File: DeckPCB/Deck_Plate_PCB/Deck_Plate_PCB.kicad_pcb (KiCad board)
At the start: 2 copper layers, 101.6 x 53.3 mm, 18 parts, among them J1 DB37_Female_MountingHoles, J2 DB15_Female_MountingHoles, P1 Digital, P10 CONN_01X01, P11 CONN_01X01, P12 CONN_01X01, P13 CONN_01X01, P2 Power, P3 Analog, P4 Analog, P5 PWM, P6 PWM, P7 Communication, P8 CONN_01X01, P9 CONN_01X01, U1 Adafruit_INA219_Breakout, U2 LM2576T-5, U3 D24V25F9

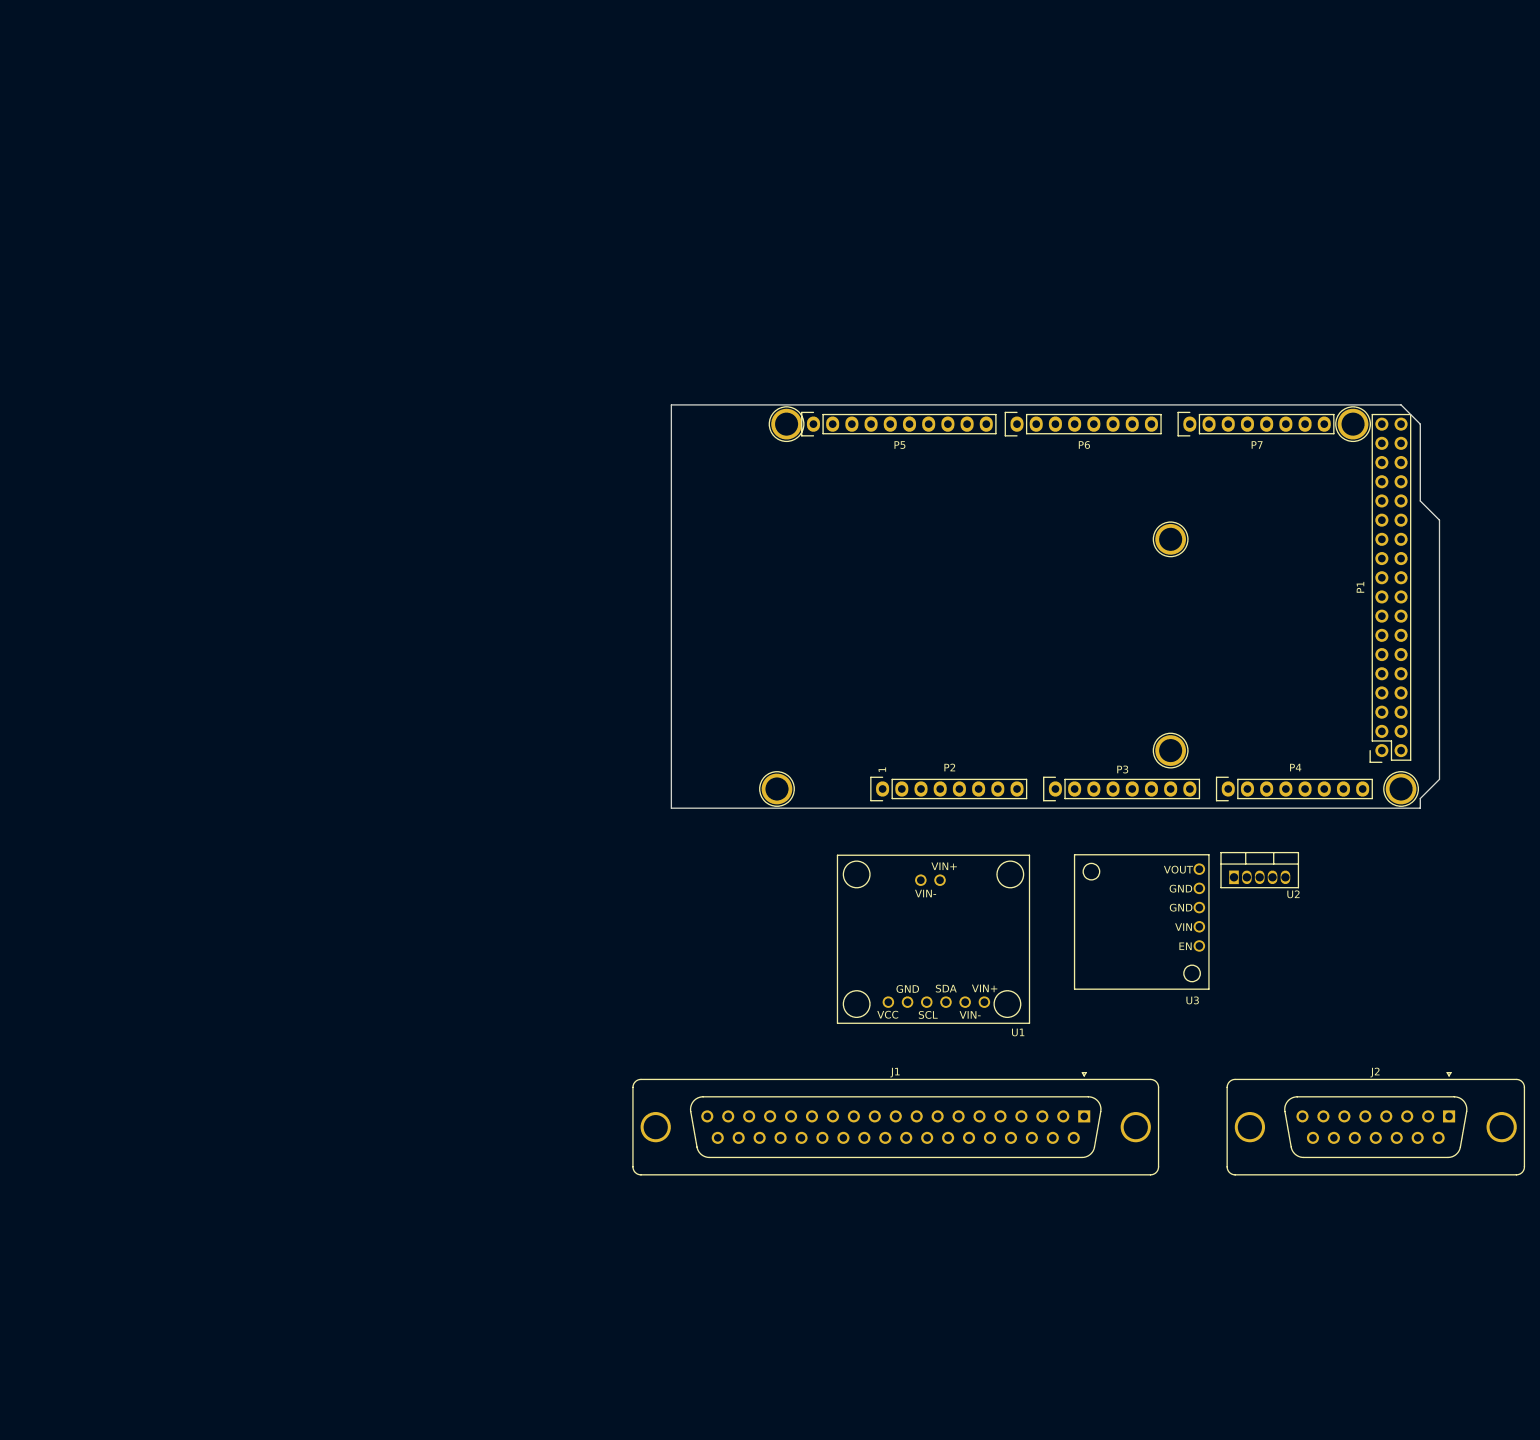
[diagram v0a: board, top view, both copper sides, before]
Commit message: Deleted OnBoardPCB folder, replaced with Deck_Plate_PCB. This should be treated as the MASTER PCB reference from here on out. Added all sensor footprints and symbols as custom parts which are part of a custom DECK_PLATE_PCB library.
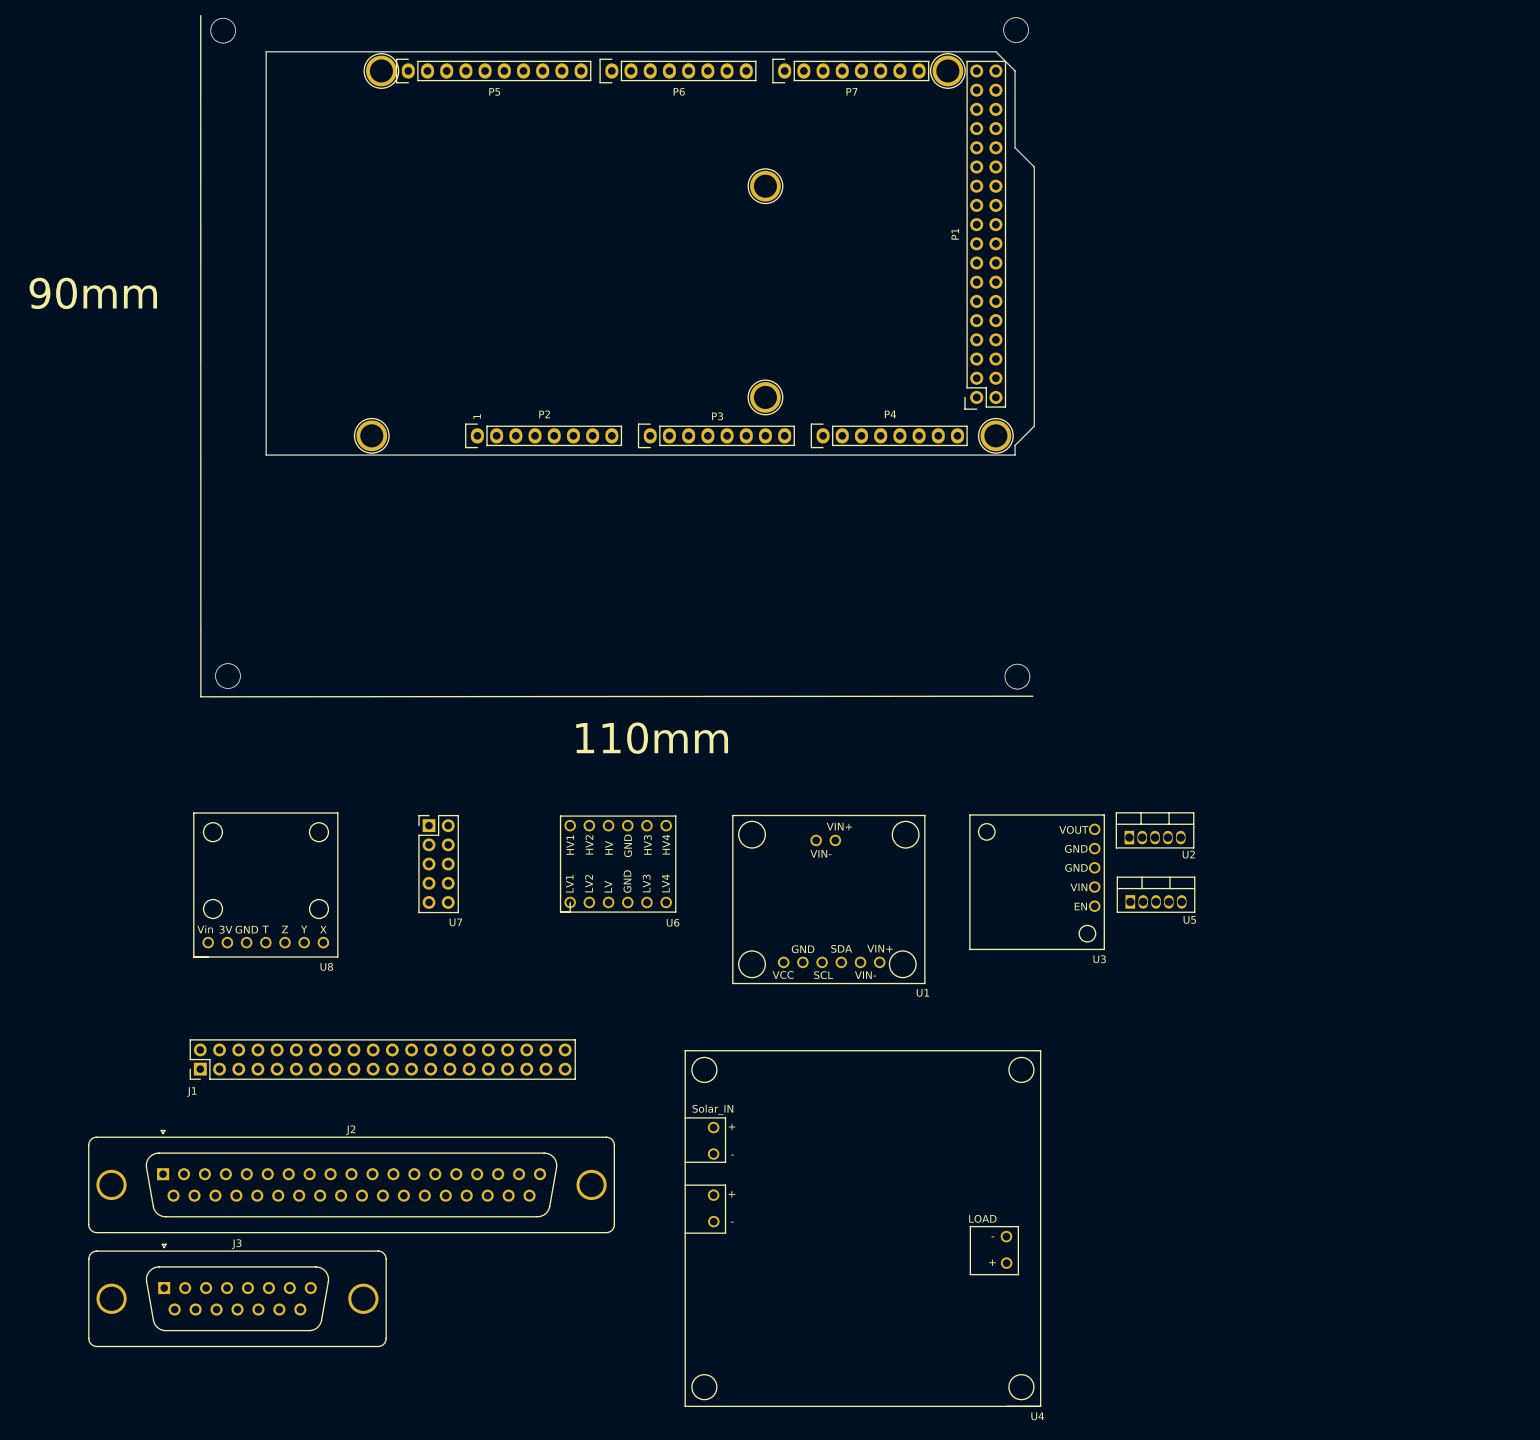
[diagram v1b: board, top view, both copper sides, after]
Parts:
- added J3: DB15_Male_MountingHoles, Connector_Dsub:DSUB-15_Male_Vertical_P2.77x2.84mm_MountingHoles, F.Cu at (36.3, 185.1)
- added U4: SunnyBuddy_Breakout, Deck_Plate_PCB:SunnyBuddy_Breakout, F.Cu at (105.2, 153.7)
- added U5: LM2576T-5, Package_TO_SOT_THT:TO-220-5_Vertical, F.Cu at (164.1, 134.1)
- added U6: SF_Logic_Level_Conv, Deck_Plate_PCB:SF_Logic_Level_Conv, F.Cu at (88.7, 135.4)
- added U7: LIDAR-LITE_V4_Range, Connector_PinHeader_2.54mm:PinHeader_2x05_P2.54mm_Vertical, F.Cu at (71.3, 124.0)
- added U8: ADXL377, Deck_Plate_PCB:ADXL337, F.Cu at (40.2, 141.4)
- J1: value DB37_Female_MountingHoles -> Raspberry_Pi_2_3; footprint Connector_Dsub:DSUB-37_Female_Vertical_P2.77x2.84mm_MountingHoles -> Connector_PinHeader_2.54mm:PinHeader_2x20_P2.54mm_Vertical
- J2: value DB15_Female_MountingHoles -> DB37_Male_MountingHoles; footprint Connector_Dsub:DSUB-15_Female_Vertical_P2.77x2.84mm_MountingHoles -> Connector_Dsub:DSUB-37_Male_Vertical_P2.77x2.84mm_MountingHoles
- moved J2 170.3 mm to (36.1, 170.1)
- moved J1 117.1 mm to (41.1, 156.2), turned to 90 degrees
- moved P2 71.1 mm to (77.7, 72.4)
- moved P4 71.1 mm to (123.4, 72.4)
- moved P5 71.1 mm to (68.6, 24.2)
- moved P6 71.1 mm to (95.5, 24.2)
- moved P9 71.1 mm to (115.8, 67.3)
- moved P1 71.1 mm to (143.8, 67.3)
- moved P10 71.1 mm to (146.3, 72.4)
- moved P11 71.1 mm to (65.0, 24.2)
- moved P12 71.1 mm to (115.8, 39.4)
- moved P13 71.1 mm to (140.0, 24.2)
- moved P3 71.1 mm to (100.6, 72.4)
- moved P7 71.1 mm to (118.4, 24.2)
- moved P8 71.1 mm to (63.8, 72.4)
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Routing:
- net (no net): vias 0 -> 4
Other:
- board text added: "110mm"
- board text added: "90mm"

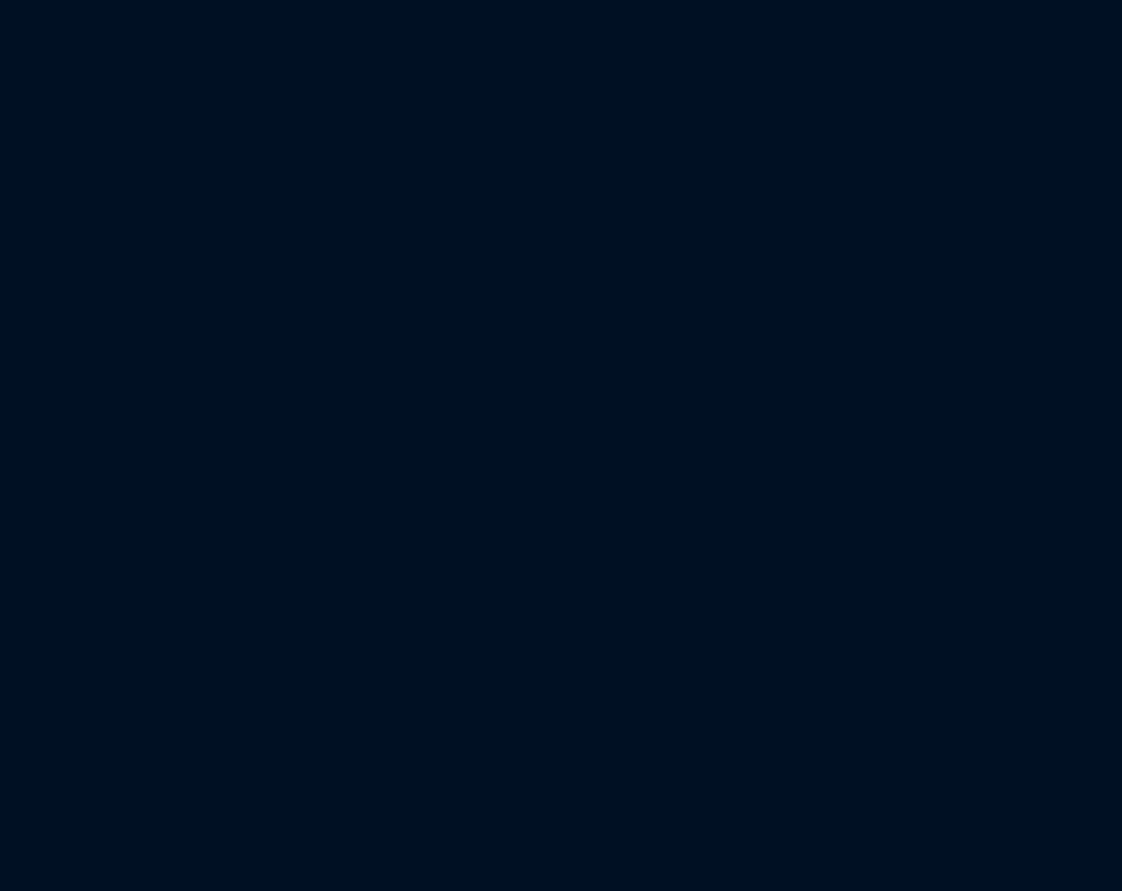
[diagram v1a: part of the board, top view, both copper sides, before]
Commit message: Finished all symbol and footprint additions. Added mounting holes for SunnyBuddy, INA219, and ADXL377. Added discrete component footprints. Defined NASA PWR and TELEMETRY pinouts.
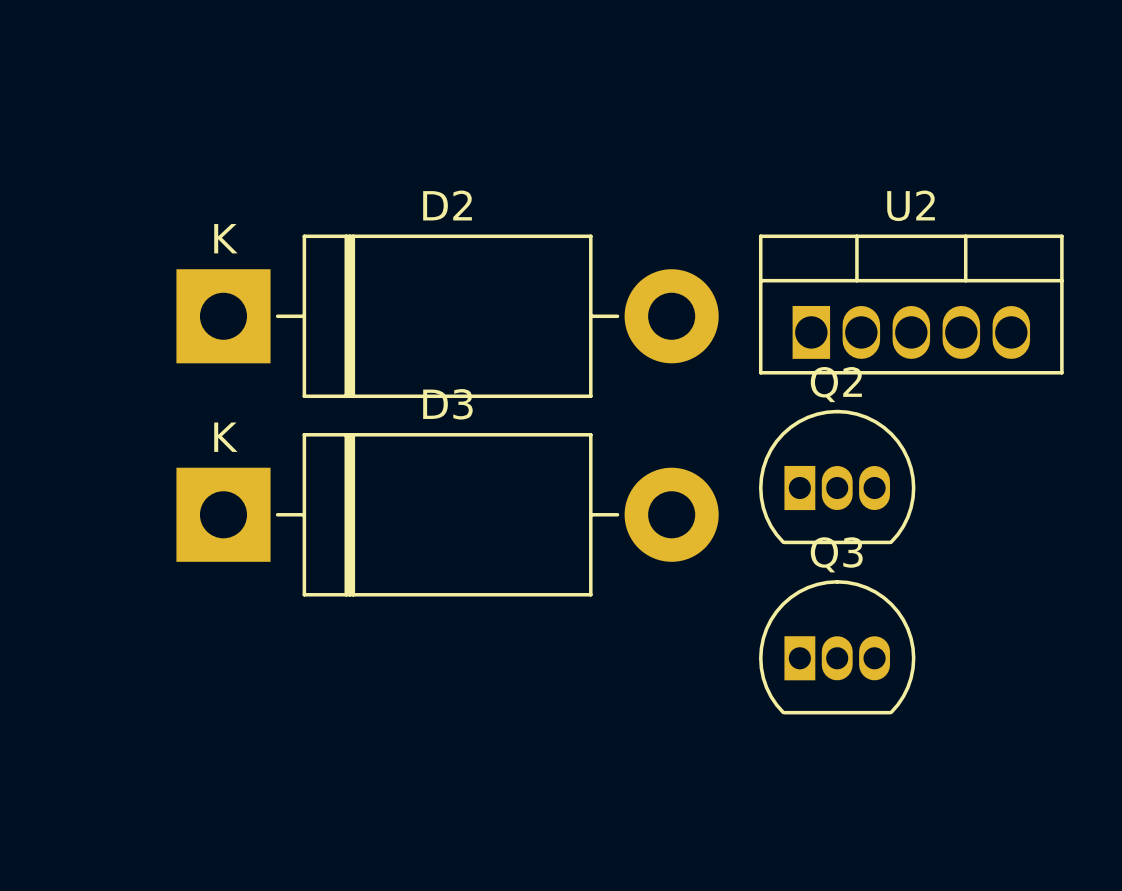
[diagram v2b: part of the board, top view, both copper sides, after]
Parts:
- added D2: 1N5822, Diode_THT:D_DO-201AD_P15.24mm_Horizontal, F.Cu at (187.5, 151.6)
- added D3: 1N5822, Diode_THT:D_DO-201AD_P15.24mm_Horizontal, F.Cu at (187.5, 158.3)
- added Q2: 2N7000, Package_TO_SOT_THT:TO-92_Inline, F.Cu at (207.1, 157.4)
- added Q3: 2N7000, Package_TO_SOT_THT:TO-92_Inline, F.Cu at (207.1, 163.2)
- added U2: LM2576T-5, Package_TO_SOT_THT:TO-220-5_Vertical, F.Cu at (207.5, 152.1)
- J3: value DB15_Male_MountingHoles -> NASA PWR_Interface
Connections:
- net Net-(J1-Pad22) renamed /Bit_16
- net Net-(J1-Pad27) renamed /Bit_1
- net Net-(J1-Pad37) renamed /Strobe
- net Net-(J1-Pad8) renamed /TTL_TX
- net Net-(J2-Pad1) renamed /Analog_1
- net Net-(J2-Pad10) renamed /Analog_10
- net Net-(J2-Pad11) renamed /Bit_1_MSB
- net Net-(J2-Pad2) renamed /Analog_2
- net Net-(J2-Pad29) renamed /Bit_16_LSB
- net Net-(J2-Pad3) renamed /Analog_3
- net Net-(J2-Pad30) renamed /Para_Strobe
- net Net-(J2-Pad32) renamed /RS_DATA
- net Net-(J2-Pad33) renamed /RS_GND
- net Net-(J2-Pad4) renamed /Analog_4
- net Net-(J2-Pad5) renamed /Analog_5
- net Net-(J2-Pad6) renamed /Analog_6
- net Net-(J2-Pad7) renamed /Analog_7
- net Net-(J2-Pad8) renamed /Analog_8
- net Net-(J2-Pad9) renamed /Analog_9
- net Net-(J3-Pad1) renamed /28V_GSE_1
- net Net-(J3-Pad10) renamed /TE-2
- net Net-(J3-Pad11) renamed /TE-3
- net Net-(J3-Pad2) renamed /TE-RA
- net Net-(J3-Pad3) renamed /TE-RB
- net Net-(J3-Pad4) renamed /TE-1
- net Net-(J3-Pad9) renamed /28V_GSE_2
- net Net-(U3-Pad5) renamed /9V_Bus
- net Net-(U4-Pad3) renamed /LED+
- net Net-(U6-Pad9) renamed /???
- J1 pad 14: Net-(J1-Pad14) -> GND
- J1 pad 15: Net-(J1-Pad15) -> /Bit_13
- J1 pad 16: Net-(J1-Pad16) -> /Bit_14
- J1 pad 18: Net-(J1-Pad18) -> /Bit_15
- J1 pad 2: Net-(J1-Pad2) -> /5V_Bus_1
- J1 pad 20: Net-(J1-Pad20) -> GND
- J1 pad 21: Net-(J1-Pad21) -> /Bit_10
- J1 pad 24: Net-(J1-Pad24) -> /Bit_9
- J1 pad 25: Net-(J1-Pad25) -> GND
- J1 pad 26: Net-(J1-Pad26) -> /Bit_8
- J1 pad 28: Net-(J1-Pad28) -> /Bit_2
- J1 pad 29: Net-(J1-Pad29) -> /Bit_6
- J1 pad 3: Net-(J1-Pad3) -> /Bit_3
- J1 pad 30: Net-(J1-Pad30) -> GND
- J1 pad 31: Net-(J1-Pad31) -> /Bit_7
- J1 pad 34: Net-(J1-Pad34) -> GND
- J1 pad 38: Net-(J1-Pad38) -> /Bit_11
- J1 pad 39: Net-(J1-Pad39) -> GND
- J1 pad 40: Net-(J1-Pad40) -> /Bit_12
- J1 pad 5: Net-(J1-Pad5) -> /Bit_4
- J1 pad 6: Net-(J1-Pad6) -> GND
- J1 pad 7: Net-(J1-Pad7) -> /Bit_5
- J1 pad 9: Net-(J1-Pad9) -> GND
- J2 pad 12: Net-(J2-Pad12) -> /Bit_2
- J2 pad 13: Net-(J2-Pad13) -> /Bit_3
- J2 pad 14: Net-(J2-Pad14) -> /Bit_4
- J2 pad 15: Net-(J2-Pad15) -> /Bit_5
- J2 pad 16: Net-(J2-Pad16) -> /Bit_6
- J2 pad 18: Net-(J2-Pad18) -> GND
- J2 pad 19: Net-(J2-Pad19) -> GND
- J2 pad 20: Net-(J2-Pad20) -> /Bit_7
- J2 pad 21: Net-(J2-Pad21) -> /Bit_8
- J2 pad 22: Net-(J2-Pad22) -> /Bit_9
- J2 pad 23: Net-(J2-Pad23) -> /Bit_10
- J2 pad 24: Net-(J2-Pad24) -> /Bit_11
- J2 pad 25: Net-(J2-Pad25) -> /Bit_12
- J2 pad 26: Net-(J2-Pad26) -> /Bit_13
- J2 pad 27: Net-(J2-Pad27) -> /Bit_14
- J2 pad 28: Net-(J2-Pad28) -> /Bit_15
- J2 pad 36: Net-(J2-Pad36) -> GND
- J2 pad 37: Net-(J2-Pad37) -> GND
- J3 pad 12: Net-(J3-Pad12) -> GND
- J3 pad 13: Net-(J3-Pad13) -> GND
- J3 pad 14: Net-(J3-Pad14) -> GND
- J3 pad 15: Net-(J3-Pad15) -> GND
- J3 pad 5: Net-(J3-Pad5) -> GND
- J3 pad 6: Net-(J3-Pad6) -> GND
- J3 pad 7: Net-(J3-Pad7) -> GND
- J3 pad 8: Net-(J3-Pad8) -> GND
- U1 pad 1: Net-(U1-Pad1) -> /5V_Bus_1
- U1 pad 2: Net-(U1-Pad2) -> GND
- U1 pad 3: Net-(U1-Pad3) -> /SCL
- U1 pad 4: Net-(U1-Pad4) -> /SDA
- U1 pad 5: Net-(U1-Pad5) -> /Solar_IN-
- U1 pad 6: Net-(U1-Pad6) -> /Solar_IN+
- U3 pad 2: Net-(U3-Pad2) -> /NASA_28V
- U3 pad 3: Net-(U3-Pad3) -> GND
- U3 pad 4: Net-(U3-Pad4) -> GND
- U4 pad 1: Net-(U4-Pad1) -> /Solar_IN+
- U4 pad 2: Net-(U4-Pad2) -> /Solar_IN-
- U4 pad 4: Net-(U4-Pad4) -> GND
- U5 pad 1: Net-(U5-Pad1) -> /NASA_28V
- U5 pad 3: Net-(U5-Pad3) -> GND
- U5 pad 4: Net-(U5-Pad4) -> /5V_Bus_1
- U5 pad 5: Net-(U5-Pad5) -> GND
- U6 pad 1: Net-(U6-Pad1) -> /2(**)
- U6 pad 10: Net-(U6-Pad10) -> GND
- U6 pad 11: Net-(U6-Pad11) -> /I2C_SCL
- U6 pad 12: Net-(U6-Pad12) -> /I2C_SDA
- U6 pad 2: Net-(U6-Pad2) -> /3(**)
- U6 pad 3: Net-(U6-Pad3) -> /5V_Bus_1
- U6 pad 4: Net-(U6-Pad4) -> GND
- U6 pad 5: Net-(U6-Pad5) -> /21(SCL)
- U6 pad 6: Net-(U6-Pad6) -> /20(SDA)
- U6 pad 7: Net-(U6-Pad7) -> /GPIO_A
- U6 pad 8: Net-(U6-Pad8) -> /GPIO_B
- U7 pad 1: Net-(U7-Pad1) -> /5V_Bus_2
- U7 pad 2: Net-(U7-Pad2) -> GND
- U7 pad 3: Net-(U7-Pad3) -> /I2C_SDA
- U7 pad 4: Net-(U7-Pad4) -> /I2C_SCL
- U7 pad 5: Net-(U7-Pad5) -> /GPIO_A
- U7 pad 6: Net-(U7-Pad6) -> /GPIO_B
- U8 pad 1: Net-(U8-Pad1) -> /5V_Bus_2
- U8 pad 3: Net-(U8-Pad3) -> GND
- U8 pad 5: Net-(U8-Pad5) -> /A0
- U8 pad 6: Net-(U8-Pad6) -> /A1
- U8 pad 7: Net-(U8-Pad7) -> /A2
